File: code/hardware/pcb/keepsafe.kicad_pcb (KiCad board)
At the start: 4 copper layers, 32 x 22 mm, 1 part

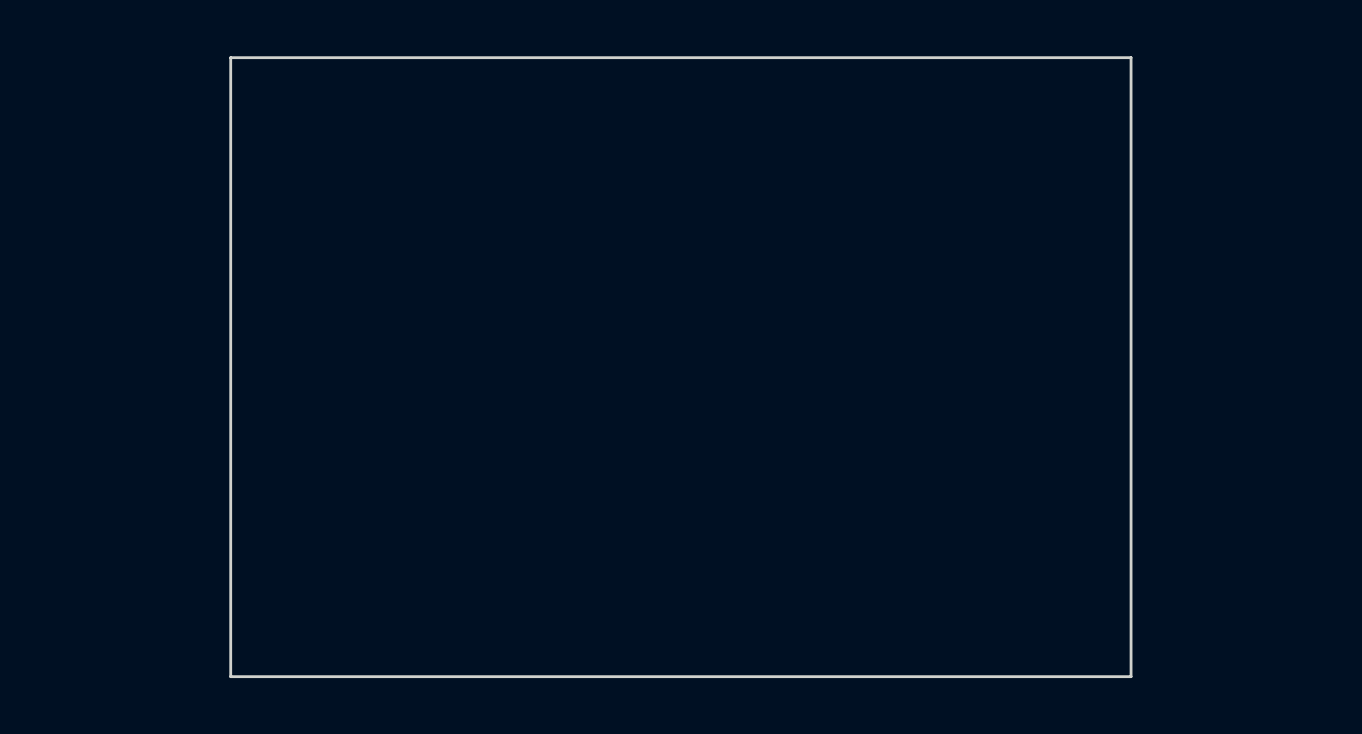
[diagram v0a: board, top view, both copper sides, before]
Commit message: PCB设计文件 + AutoGen团队脚本更新
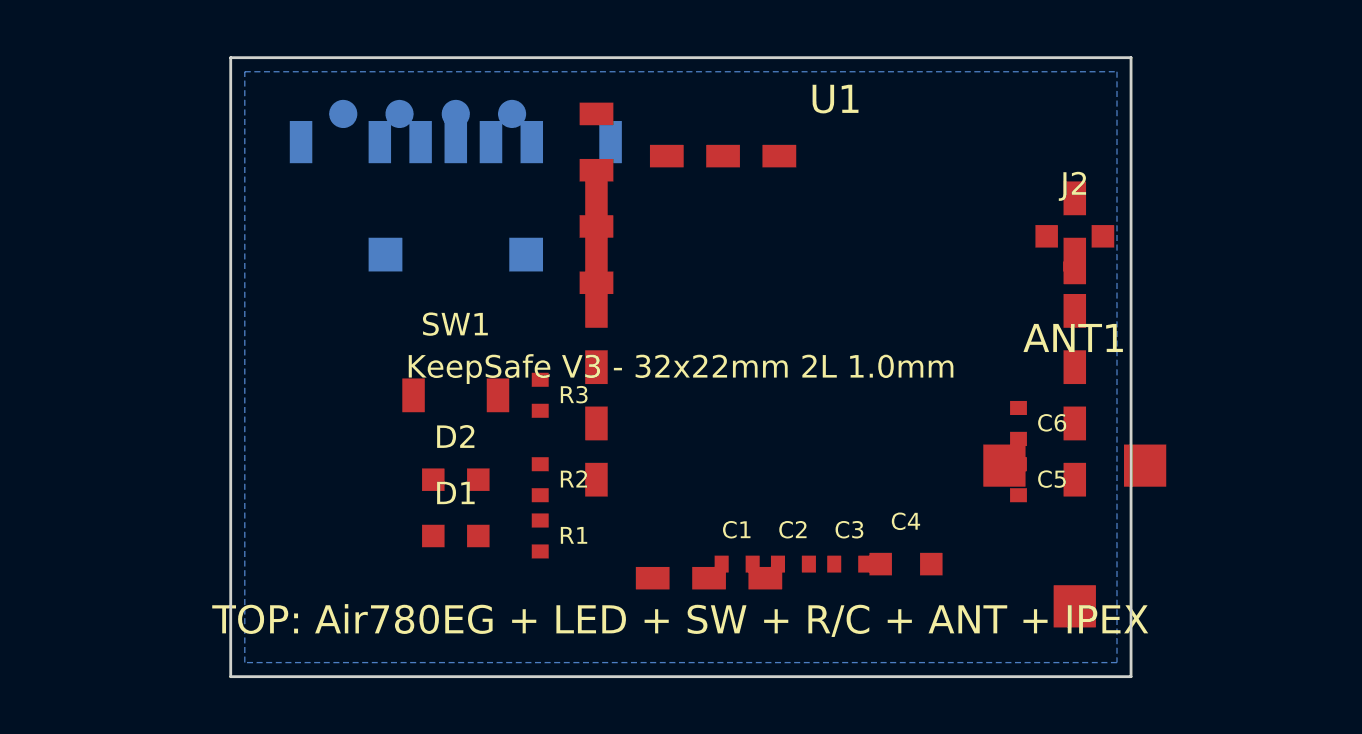
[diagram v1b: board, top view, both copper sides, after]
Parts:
- removed the ? at (0.00, 0.00)
- added ?: , PCB_Outline_32x22mm, Edge.Cuts at (0.00, 0.00)
- added ANT1: GPS_ANT, KeepSafe:GPS_ANT_12x12mm, F.Cu at (14.0, 6.00)
- added BZ1: Buzzer, KeepSafe:Buzzer_8.5mm_SMD, B.Cu at (-8.00, -4.00)
- added C1: 100nF, KeepSafe:C_0402, F.Cu at (2.00, 7.00)
- added C2: 100nF, KeepSafe:C_0402, F.Cu at (4.00, 7.00)
- added C3: 100nF, KeepSafe:C_0402, F.Cu at (6.00, 7.00)
- added C4: 10uF, KeepSafe:C_0603, F.Cu at (8.00, 7.00)
- added C5: 22pF, KeepSafe:C_0402, F.Cu at (12.0, 4.00)
- added C6: 22pF, KeepSafe:C_0402, F.Cu at (12.0, 2.00)
- added D1: RED, KeepSafe:LED_0603, F.Cu at (-8.00, 6.00)
- added D2: GRN, KeepSafe:LED_0603, F.Cu at (-8.00, 4.00)
- added J1: SIM_Nano, KeepSafe:SIM_Nano_PushPull, B.Cu at (-8.00, -3.00)
- added J2: IPEX1, KeepSafe:IPEX1_UFL, F.Cu at (14.0, -4.00)
- added J3: BAT_2P, KeepSafe:Battery_1.25mm_2P, B.Cu at (-8.00, -8.00)
- added R1: 10K, KeepSafe:R_0402, F.Cu at (-5.00, 6.00)
- added R2: 10K, KeepSafe:R_0402, F.Cu at (-5.00, 4.00)
- added R3: 10K, KeepSafe:R_0402, F.Cu at (-5.00, 1.00)
- added SW1: SW, KeepSafe:SW_3x4x2.5, F.Cu at (-8.00, 1.00)
- added TP1: UART1_TX, KeepSafe:TestPoint_1mm, B.Cu at (-12.0, -9.00)
- added TP2: UART1_RX, KeepSafe:TestPoint_1mm, B.Cu at (-10.0, -9.00)
- added TP3: USB_DP, KeepSafe:TestPoint_1mm, B.Cu at (-8.00, -9.00)
- added TP4: USB_DM, KeepSafe:TestPoint_1mm, B.Cu at (-6.00, -9.00)
- added U1: Air780EG, KeepSafe:LGA-109, F.Cu at (5.50, 0.00)
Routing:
- added copper zone on B.Cu, net GND
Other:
- copper layers 4 -> 2
- board text added: "BOT: SIM + Buzzer + Battery + TestPoints"
- board text added: "KeepSafe V3 - 32x22mm 2L 1.0mm"
- board text added: "TOP: Air780EG + LED + SW + R/C + ANT + IPEX"
